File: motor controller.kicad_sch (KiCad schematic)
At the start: 55 parts, among them J1 Servo Header, J2 XT30, J3 Ext Power, J4 USB_PWR, J5 USB Header, J6 M0, J7 M1, J8 M2, J9 M3, M0-BUF1 SN74LVC2G14, M0DA1 LED, M0DB1 LED, M0R1 R_Small, M0R2 R_Small, M1-BUF1 SN74LVC2G14, M1DA1 LED, M1DB1 LED, M1R1 R_Small, M1R2 R_Small, M2-BUF1 SN74LVC2G14, M2DA1 LED, M2DB1 LED, M2R1 R_Small, M2R2 R_Small, M3-BUF1 SN74LVC2G14, M3DA1 LED, M3DB1 LED, M3R1 R_Small, M3R2 R_Small, SW1 SW_Push

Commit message: updated schematic and pcb
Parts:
- J3: footprint Connector_AMASS:AMASS_XT30PW-M_1x02_P2.50mm_Horizontal -> Connector_JST:JST_XH_S3B-XH-A_1x03_P2.50mm_Horizontal
- M0DA1: footprint LED_SMD:LED_0805_2012Metric_Pad1.15x1.40mm_HandSolder -> LED_SMD:LED_0805_2012Metric
- SW1: value SW_Push -> RESET
- U1: renamed from IFX9201SG1; value M1 -> M1-IFX9201SG
- U2: renamed from IFX9201SG2; value M3 -> M3-IFX9201SG
- U3: renamed from IFX9201SG3; value M2 -> M2-IFX9201SG
- U4: renamed from IFX9201SG4; value M0 -> M0-IFX9201SG
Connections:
- net M0-Enc-A: now also M0-BUF1.3 (2A); no longer M0-BUF1.1 (1A)
- net M0-Enc-B: now also M0-BUF1.1 (1A); no longer M0-BUF1.3 (2A)
- net M1-Enc-A: now also M1-BUF1.3 (2A); no longer M1-BUF1.1 (1A)
- net M1-Enc-B: now also M1-BUF1.1 (1A); no longer M1-BUF1.3 (2A)
- net M2-Enc-A: now also M2-BUF1.3 (2A); no longer M2-BUF1.1 (1A)
- net M2-Enc-B: now also M2-BUF1.1 (1A); no longer M2-BUF1.3 (2A)
- net M3-A: now also C19.2; no longer C20.1
- net M3-B: now also C20.1; no longer C19.2
- net M3-Enc-A: now also M3-BUF1.3 (2A); no longer M3-BUF1.1 (1A)
- net M3-Enc-B: now also M3-BUF1.1 (1A); no longer M3-BUF1.3 (2A)
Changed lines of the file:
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@@
 		)
 	)
-	(global_label "M3-Enc-B"
+	(global_label "M3-Enc-A"
 		(shape input)
 		(at 90.17 177.8 180)
@@
 		)
 		(property "Intersheetrefs" "${INTERSHEET_REFS}"
-			(at 76.7225 177.8 0)
+			(at 76.9039 177.8 0)
 			(effects
 				(font
@@
 		)
 	)
-	(global_label "M0-Enc-A"
+	(global_label "M0-Enc-B"
 		(shape input)
 		(at 31.75 137.16 180)
@@
 		)
 		(property "Intersheetrefs" "${INTERSHEET_REFS}"
-			(at 18.4839 137.16 0)
+			(at 18.3025 137.16 0)
 			(effects
 				(font
@@
 		)
 	)
-	(global_label "M1-Enc-B"
+	(global_label "M1-Enc-A"
 		(shape input)
 		(at 90.17 142.24 180)
@@
 		)
 		(property "Intersheetrefs" "${INTERSHEET_REFS}"
-			(at 76.7225 142.24 0)
+			(at 76.9039 142.24 0)
 			(effects
 				(font
@@
 		)
 	)
-	(global_label "M3-B"
+	(global_label "M3-A"
 		(shape input)
 		(at 273.05 143.51 270)
@@
 		)
 		(property "Intersheetrefs" "${INTERSHEET_REFS}"
-			(at 273.05 151.9985 90)
+			(at 273.05 151.8171 90)
 			(effects
 				(font
@@
 		)
 	)
-	(global_label "M3-A"
+	(global_label "M3-B"
 		(shape input)
 		(at 276.86 143.51 270)
@@
 		)
 		(property "Intersheetrefs" "${INTERSHEET_REFS}"
-			(at 276.86 151.8171 90)
+			(at 276.86 151.9985 90)
 			(effects
 				(font
@@
 		)
 	)
-	(global_label "M1-Enc-A"
+	(global_label "M1-Enc-B"
 		(shape input)
 		(at 90.17 137.16 180)
@@
 		)
 		(property "Intersheetrefs" "${INTERSHEET_REFS}"
-			(at 76.9039 137.16 0)
+			(at 76.7225 137.16 0)
 			(effects
 				(font
@@
 		)
 	)
-	(global_label "M2-Enc-A"
+	(global_label "M2-Enc-B"
 		(shape input)
 		(at 31.75 172.72 180)
@@
 		)
 		(property "Intersheetrefs" "${INTERSHEET_REFS}"
-			(at 18.4839 172.72 0)
+			(at 18.3025 172.72 0)
 			(effects
 				(font
@@
 		)
 	)
-	(global_label "M0-Enc-B"
+	(global_label "M0-Enc-A"
 		(shape input)
 		(at 31.75 142.24 180)
@@
 		)
 		(property "Intersheetrefs" "${INTERSHEET_REFS}"
-			(at 18.3025 142.24 0)
+			(at 18.4839 142.24 0)
 			(effects
 				(font
@@
 		)
 	)
-	(global_label "M3-Enc-A"
+	(global_label "M3-Enc-B"
 		(shape input)
 		(at 90.17 172.72 180)
@@
 		)
 		(property "Intersheetrefs" "${INTERSHEET_REFS}"
-			(at 76.9039 172.72 0)
+			(at 76.7225 172.72 0)
 			(effects
 				(font
@@
 		)
 	)
-	(global_label "M2-Enc-B"
+	(global_label "M2-Enc-A"
 		(shape input)
 		(at 31.75 177.8 180)
@@
 		)
 		(property "Intersheetrefs" "${INTERSHEET_REFS}"
-			(at 18.3025 177.8 0)
+			(at 18.4839 177.8 0)
 			(effects
 				(font
@@
 		(on_board yes)
 		(dnp no)
-		(property "Reference" "IFX9201SG3"
+		(property "Reference" "U3"
 			(at 240.03 35.56 0)
 			(effects
@@
 			)
 		)
-		(property "Value" "M2"
+		(property "Value" "M2-IFX9201SG"
 			(at 240.03 52.07 0)
 			(effects
@@
 			(project "motor controller"
 				(path "/0d2d01d1-eff8-45cb-a873-0719ff148ee4"
-					(reference "IFX9201SG3")
+					(reference "U3")
 					(unit 1)
 				)
@@
 			)
 		)
-		(property "Footprint" "LED_SMD:LED_0805_2012Metric_Pad1.15x1.40mm_HandSolder"
+		(property "Footprint" "LED_SMD:LED_0805_2012Metric"
 			(at 64.77 132.08 0)
 			(effects
@@
 		(on_board yes)
 		(dnp no)
-		(property "Reference" "IFX9201SG4"
+		(property "Reference" "U4"
 			(at 240.03 85.09 0)
 			(effects
@@
 			)
 		)
-		(property "Value" "M0"
+		(property "Value" "M0-IFX9201SG"
 			(at 240.03 101.6 0)
 			(effects
@@
 			(project ""
 				(path "/0d2d01d1-eff8-45cb-a873-0719ff148ee4"
-					(reference "IFX9201SG4")
+					(reference "U4")
 					(unit 1)
 				)
@@
 		(on_board yes)
 		(dnp no)
-		(property "Reference" "IFX9201SG2"
+		(property "Reference" "U2"
 			(at 62.23 35.56 0)
 			(effects
@@
 			)
 		)
-		(property "Value" "M3"
+		(property "Value" "M3-IFX9201SG"
 			(at 62.23 52.07 0)
 			(effects
@@
 			(project "motor controller"
 				(path "/0d2d01d1-eff8-45cb-a873-0719ff148ee4"
-					(reference "IFX9201SG2")
+					(reference "U2")
 					(unit 1)
 				)
@@
 		(on_board yes)
 		(dnp no)
-		(property "Reference" "IFX9201SG1"
+		(property "Reference" "U1"
 			(at 60.96 85.09 0)
 			(effects
@@
 			)
 		)
-		(property "Value" "M1"
+		(property "Value" "M1-IFX9201SG"
 			(at 60.96 101.6 0)
 			(effects
@@
 			(project "motor controller"
 				(path "/0d2d01d1-eff8-45cb-a873-0719ff148ee4"
-					(reference "IFX9201SG1")
+					(reference "U1")
 					(unit 1)
 				)
@@
 			)
 		)
-		(property "Value" "SW_Push"
+		(property "Value" "RESET"
 			(at 154.94 118.11 0)
 			(effects
@@
 			)
 		)
-		(property "Footprint" "Connector_AMASS:AMASS_XT30PW-M_1x02_P2.50mm_Horizontal"
+		(property "Footprint" "Connector_JST:JST_XH_S3B-XH-A_1x03_P2.50mm_Horizontal"
 			(at 149.86 142.24 0)
 			(effects

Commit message: changes suggested by Rob
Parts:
- removed C1, C10, C9: 100uF, Capacitor_THT:CP_Radial_D6.3mm_P2.50mm, symbol Device:C_Polarized_Small_US
- removed C17, C18, C19, C20: 10n, Capacitor_SMD:C_1206_3216Metric, symbol Device:C_Small
- C11, C12, C13, C14, C3, C4, C5, C6: value 100n -> 22n
- C15, C16, C7, C8: value 10n -> 22n
- renumbered M3-BUF1 to U5, M0-BUF1 to U6, M2-BUF1 to U7, M1-BUF1 to U8
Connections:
- net +VM is gone; now on net GND: C11.1, C12.1, C2.1, C3.1, C4.1, J2.2 (+), U1.4 (VS), U2.4 (VS), U3.4 (VS), U4.4 (VS)
- net 5v: no longer J3.2 (5v), U5.5 (V_{CC}), U6.5 (V_{CC}), U7.5 (V_{CC}), U8.5 (V_{CC})
- net GND: now also C13.1, C14.1, C15.1, C16.1, C5.2, C6.2, C7.2, C8.2; no longer C2.2, J2.1 (-)
- net M0-A: now also J6.6 (Pin_6); no longer C8.1
- net M0-B: now also J6.5 (Pin_5); no longer C7.2
- net M1-A: now also J7.6 (Pin_6); no longer C16.1
- net M1-B: now also J7.5 (Pin_5); no longer C15.2
- net M2-A: now also J8.6 (Pin_6)
- net M2-B: now also J8.5 (Pin_5)
- net M3-A: now also J9.5 (Pin_5)
- net M3-B: now also J9.6 (Pin_6)
- net M3-Enc-B: no longer J9.1 (Pin_1)
- net +3V3: now reaches C14.2, U3.2 (VSO)
- net +3V3: now also A1.36 (3V3), C13.2, C15.2, C16.2, C5.1, C6.1, C7.1, C8.1, U1.2 (VSO), U2.2 (VSO), U4.2 (VSO), U5.5 (V_{CC}), U6.5 (V_{CC}), U7.5 (V_{CC}), U8.5 (V_{CC})
- net 12v renamed +12V
- removed net 3.3v: A1.36 (3V3), C13.1, C14.1, C5.1, C6.1
- new net: C2.2, J2.1 (-)
- new net +5V: J3.2 (5v)
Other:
- moved on the sheet: J2

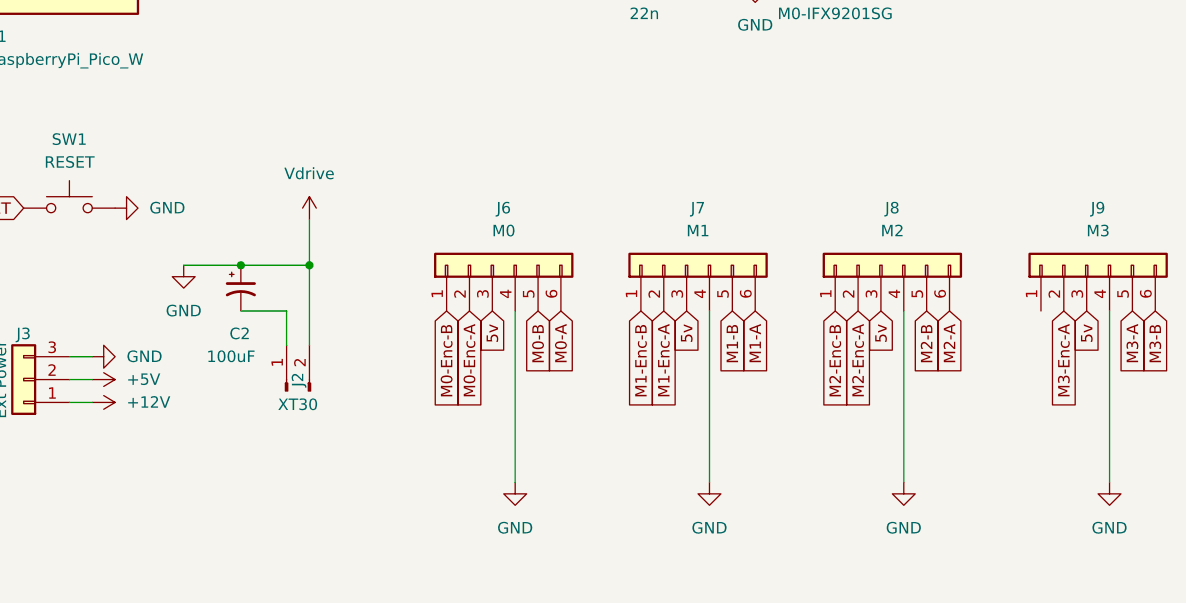
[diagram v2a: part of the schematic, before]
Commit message: fixed a short, started updating the PCB layout
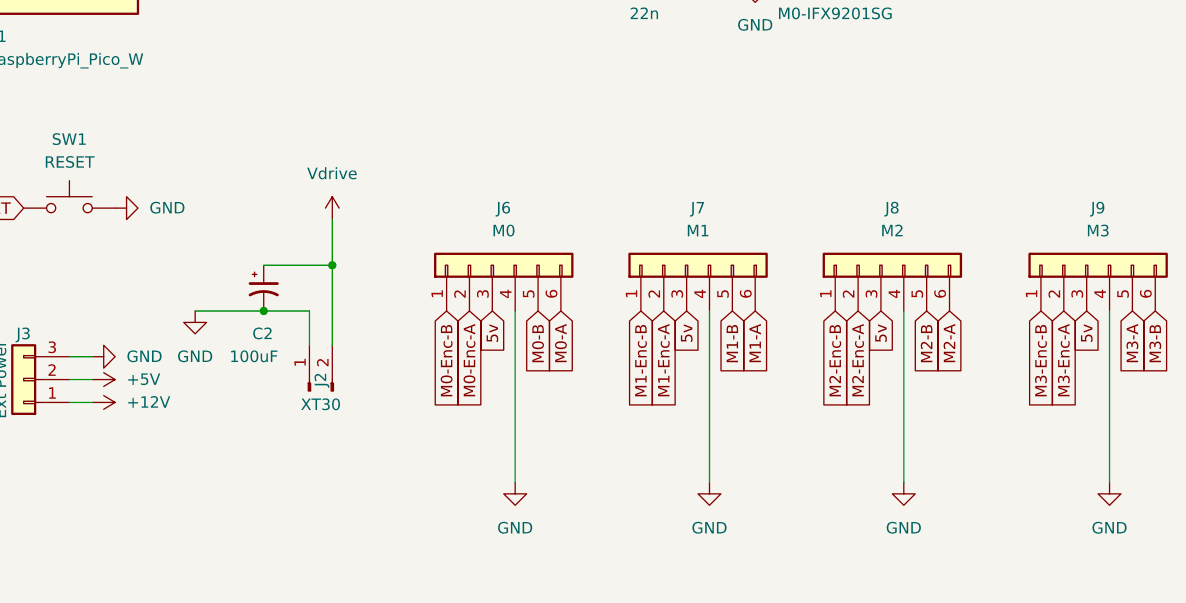
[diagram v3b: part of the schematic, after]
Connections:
- net GND: now also C2.2, J2.1 (-); no longer C11.1, C12.1, C2.1, C3.1, C4.1, J2.2 (+), U1.4 (VS), U2.4 (VS), U3.4 (VS), U4.4 (VS)
- net M3-Enc-B: now also J9.1 (Pin_1)
- new net Vdrive: C11.1, C12.1, C2.1, C3.1, C4.1, J2.2 (+), U1.4 (VS), U2.4 (VS), U3.4 (VS), U4.4 (VS)
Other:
- moved on the sheet: C2, J2
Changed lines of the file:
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@@
 	)
 	(junction
+		(at 176.53 134.62)
+		(diameter 0)
+		(color 0 0 0 0)
+	)
+	(junction
 		(at 218.44 90.17)
 		(diameter 0)
@@
 	)
 	(junction
-		(at 173.99 129.54)
-		(diameter 0)
-		(color 0 0 0 0)
-	)
-	(junction
 		(at 39.37 40.64)
 		(diameter 0)
@@
 	)
 	(junction
-		(at 181.61 129.54)
+		(at 184.15 129.54)
 		(diameter 0)
 		(color 0 0 0 0)
@@
 	(wire
 		(pts
-			(xy 181.61 138.43) (xy 181.61 129.54)
+			(xy 184.15 138.43) (xy 184.15 129.54)
 		)
 		(stroke
@@
 	(wire
 		(pts
-			(xy 181.61 129.54) (xy 181.61 124.46)
+			(xy 184.15 129.54) (xy 184.15 124.46)
 		)
 		(stroke
@@
 	(wire
 		(pts
-			(xy 167.64 129.54) (xy 173.99 129.54)
-		)
-		(stroke
-			(width 0)
-			(type default)
-		)
-	)
-	(wire
-		(pts
 			(xy 111.76 142.24) (xy 111.76 147.32)
 		)
@@
 	(wire
 		(pts
-			(xy 179.07 134.62) (xy 173.99 134.62)
+			(xy 181.61 134.62) (xy 176.53 134.62)
 		)
 		(stroke
@@
 	(wire
 		(pts
-			(xy 179.07 138.43) (xy 179.07 134.62)
+			(xy 168.91 134.62) (xy 176.53 134.62)
+		)
+		(stroke
+			(width 0)
+			(type default)
+		)
+	)
+	(wire
+		(pts
+			(xy 181.61 138.43) (xy 181.61 134.62)
 		)
 		(stroke
@@
 	(wire
 		(pts
-			(xy 173.99 129.54) (xy 181.61 129.54)
+			(xy 176.53 129.54) (xy 184.15 129.54)
 		)
 		(stroke
@@
 		)
 	)
+	(global_label "M3-Enc-B"
+		(shape input)
+		(at 262.89 134.62 270)
+		(fields_autoplaced yes)
+		(effects
+			(font
+				(size 1.27 1.27)
+			)
+			(justify right)
+		)
+		(property "Intersheetrefs" "${INTERSHEET_REFS}"
+			(at 262.89 148.0675 90)
+			(effects
+				(font
+					(size 1.27 1.27)
+				)
+				(justify right)
+				(hide yes)
+			)
+		)
+	)
 	(global_label "PICO RX"
 		(shape input)
@@
 	(symbol
 		(lib_id "power:GND")
-		(at 167.64 129.54 0)
+		(at 168.91 134.62 0)
 		(unit 1)
 		(exclude_from_sim no)
@@
 		(fields_autoplaced yes)
 		(property "Reference" "#PWR045"
-			(at 167.64 135.89 0)
+			(at 168.91 140.97 0)
 			(effects
 				(font
@@
 		)
 		(property "Value" "GND"
-			(at 167.64 134.62 0)
+			(at 168.91 139.7 0)
 			(effects
 				(font
@@
 		)
 		(property "Footprint" ""
-			(at 167.64 129.54 0)
+			(at 168.91 134.62 0)
 			(effects
 				(font
@@
 		)
 		(property "Datasheet" ""
-			(at 167.64 129.54 0)
+			(at 168.91 134.62 0)
 			(effects
 				(font
@@
 		)
 		(property "Description" "Power symbol creates a global label with name \"GND\" , ground"
-			(at 167.64 129.54 0)
+			(at 168.91 134.62 0)
 			(effects
 				(font
@@
 	(symbol
 		(lib_id "power:Vdrive")
-		(at 181.61 124.46 0)
+		(at 184.15 124.46 0)
 		(unit 1)
 		(exclude_from_sim no)
@@
 		(fields_autoplaced yes)
 		(property "Reference" "#PWR046"
-			(at 181.61 128.27 0)
+			(at 184.15 128.27 0)
 			(effects
 				(font
@@
 		)
 		(property "Value" "Vdrive"
-			(at 181.61 119.38 0)
+			(at 184.15 119.38 0)
 			(effects
 				(font
@@
 		)
 		(property "Footprint" ""
-			(at 181.61 124.46 0)
+			(at 184.15 124.46 0)
 			(effects
 				(font
@@
 		)
 		(property "Datasheet" ""
-			(at 181.61 124.46 0)
+			(at 184.15 124.46 0)
 			(effects
 				(font
@@
 		)
 		(property "Description" "Power symbol creates a global label with name \"Vdrive\""
-			(at 181.61 124.46 0)
+			(at 184.15 124.46 0)
 			(effects
 				(font
@@
 	(symbol
 		(lib_id "Connector:Conn_01x02_Pin")
-		(at 179.07 143.51 90)
+		(at 181.61 143.51 90)
 		(unit 1)
 		(exclude_from_sim no)
@@
 		(dnp no)
 		(property "Reference" "J2"
-			(at 180.34 142.24 0)
+			(at 182.88 142.24 0)
 			(effects
 				(font
@@
 		)
 		(property "Value" "XT30"
-			(at 180.34 145.034 90)
+			(at 182.88 145.034 90)
 			(effects
 				(font
@@
 		)
 		(property "Footprint" "Connector_AMASS:AMASS_XT30PW-M_1x02_P2.50mm_Horizontal"
-			(at 179.07 143.51 0)
+			(at 181.61 143.51 0)
 			(effects
 				(font
@@
 		)
 		(property "Datasheet" "~"
-			(at 179.07 143.51 0)
+			(at 181.61 143.51 0)
 			(effects
 				(font
@@
 		)
 		(property "Description" "XT30"
-			(at 179.07 143.51 0)
+			(at 181.61 143.51 0)
 			(effects
 				(font
@@
 	(symbol
 		(lib_id "Device:C_Polarized_Small_US")
-		(at 173.99 132.08 0)
+		(at 176.53 132.08 0)
 		(unit 1)
 		(exclude_from_sim no)
@@
 		(dnp no)
 		(property "Reference" "C2"
-			(at 172.72 137.16 0)
+			(at 175.26 137.16 0)
 			(effects
 				(font
@@
 		)
 		(property "Value" "100uF"
-			(at 170.18 139.7 0)
+			(at 172.72 139.7 0)
 			(effects
 				(font
@@
 		)
 		(property "Footprint" "Capacitor_THT:CP_Radial_D6.3mm_P2.50mm"
-			(at 173.99 132.08 0)
+			(at 176.53 132.08 0)
 			(effects
 				(font
@@
 		)
 		(property "Datasheet" "~"
-			(at 173.99 132.08 0)
+			(at 176.53 132.08 0)
 			(effects
 				(font
@@
 		)
 		(property "Description" "Polarized capacitor, small US symbol"
-			(at 173.99 132.08 0)
+			(at 176.53 132.08 0)
 			(effects
 				(font

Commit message: more tweaking
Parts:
- removed C3, C4, C7, C8: 22n, Capacitor_SMD:C_1206_3216Metric, symbol Device:C_Small
- added C10, C13, C5, C6: 22n, Capacitor_SMD:C_1206_3216Metric, symbol Device:C_Small
- renumbered C13 to C1, C15 to C2, C5 to C3, C6 to C4, C14 to C7, C16 to C8, C2 to C9, J3 to J2, J4 to J3, J5 to J4, J2 to J5, U6 to U1, U7 to U2, U2 to U3, U1 to U4, U8 to U5, U5 to U6, U3 to U7, U4 to U8
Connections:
- net +12V: now also J1.2 (Pin_2); no longer J1.1 (Pin_1)
- net +3V3: now also C11.1, C10.1
- net ADC: now also J1.3 (Pin_3); no longer J1.4 (Pin_4)
- net GND: now also C12.1, J1.1 (Pin_1), C10.2, C13.1, C5.1, C6.1; no longer C12.2, J1.2 (Pin_2)
- net GPIO16: now also M0R2.1, U1.4 (2Y); no longer M0R1.1, U1.6 (1Y)
- net GPIO17: now also M0R1.1, U1.6 (1Y); no longer M0R2.1, U1.4 (2Y)
- net GPIO21: now also M2R1.1, U2.6 (1Y); no longer M2R2.1, U2.4 (2Y)
- net GPIO22: now also M2R2.1, U2.4 (2Y); no longer M2R1.1, U2.6 (1Y)
- net M0-A: now also J6.5 (Pin_5); no longer J6.6 (Pin_6)
- net M0-B: now also J6.6 (Pin_6); no longer J6.5 (Pin_5)
- net M1-A: now also J7.5 (Pin_5); no longer J7.6 (Pin_6)
- net M1-B: now also J7.6 (Pin_6); no longer J7.5 (Pin_5)
- net M1-DIR: now also A1.14 (GPIO10); no longer A1.15 (GPIO11)
- net M1-DIS: now also A1.16 (GPIO12); no longer A1.14 (GPIO10)
- net M1-PWM: now also A1.15 (GPIO11); no longer A1.16 (GPIO12)
- net M1-SO: now also U8.8 (SI)
- net M2-SO: now also U8.3 (SO); no longer U3.8 (SI)
- net SERVO: now also J1.4 (Pin_4); no longer J1.3 (Pin_3)
- net Vdrive: now also C12.2, C13.2, C5.2, C6.2; no longer C11.1, C12.1
- net VBUS: now reaches A1.40 (VBUS), J3.2 (Pin_2)
- net VBUS: now also J6.3 (Pin_3), J7.3 (Pin_3), J8.3 (Pin_3), J9.3 (Pin_3)
- net +5V renamed +5Vext
- net +5Vext: now also J3.3 (Pin_3)
- removed net 5v: J3.3 (Pin_3), J6.3 (Pin_3), J7.3 (Pin_3), J8.3 (Pin_3), J9.3 (Pin_3)
- net M0-SO renamed M3-SO
- net M3-SO: now also U3.3 (SO); no longer U8.3 (SO)
- net PICO RX renamed PICO-RX
- net PICO-RX: no longer U3.3 (SO)
- net PICO TX renamed PICO-TX
- net PICO-TX: now also U3.8 (SI); no longer U8.8 (SI)
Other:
- moved on the sheet: C3, C4, U3, U4, U7, U8

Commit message: switched to vertical plugs
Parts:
- J1, J4: footprint Connector_JST:JST_XH_S4B-XH-A_1x04_P2.50mm_Horizontal -> Connector_JST:JST_XH_B4B-XH-AM_1x04_P2.50mm_Vertical
- J2: footprint Connector_JST:JST_XH_S3B-XH-A_1x03_P2.50mm_Horizontal -> Connector_JST:JST_XH_B3B-XH-AM_1x03_P2.50mm_Vertical
- J6, J7, J8, J9: footprint Connector_JST:JST_XH_S6B-XH-A_1x06_P2.50mm_Horizontal -> Connector_JST:JST_XH_B6B-XH-AM_1x06_P2.50mm_Vertical
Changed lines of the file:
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@@
 			)
 		)
-		(property "Footprint" "Connector_JST:JST_XH_S6B-XH-A_1x06_P2.50mm_Horizontal"
+		(property "Footprint" "Connector_JST:JST_XH_B6B-XH-AM_1x06_P2.50mm_Vertical"
 			(at 267.97 129.54 0)
 			(effects
@@
 			)
 		)
-		(property "Footprint" "Connector_JST:JST_XH_S6B-XH-A_1x06_P2.50mm_Horizontal"
+		(property "Footprint" "Connector_JST:JST_XH_B6B-XH-AM_1x06_P2.50mm_Vertical"
 			(at 245.11 129.54 0)
 			(effects
@@
 			)
 		)
-		(property "Footprint" "Connector_JST:JST_XH_S4B-XH-A_1x04_P2.50mm_Horizontal"
+		(property "Footprint" "Connector_JST:JST_XH_B4B-XH-AM_1x04_P2.50mm_Vertical"
 			(at 179.07 27.94 0)
 			(effects
@@
 			)
 		)
-		(property "Footprint" "Connector_JST:JST_XH_S6B-XH-A_1x06_P2.50mm_Horizontal"
+		(property "Footprint" "Connector_JST:JST_XH_B6B-XH-AM_1x06_P2.50mm_Vertical"
 			(at 201.93 129.54 0)
 			(effects
@@
 			)
 		)
-		(property "Footprint" "Connector_JST:JST_XH_S4B-XH-A_1x04_P2.50mm_Horizontal"
+		(property "Footprint" "Connector_JST:JST_XH_B4B-XH-AM_1x04_P2.50mm_Vertical"
 			(at 101.6 93.98 0)
 			(effects
@@
 			)
 		)
-		(property "Footprint" "Connector_JST:JST_XH_S3B-XH-A_1x03_P2.50mm_Horizontal"
+		(property "Footprint" "Connector_JST:JST_XH_B3B-XH-AM_1x03_P2.50mm_Vertical"
 			(at 149.86 142.24 0)
 			(effects
@@
 			)
 		)
-		(property "Footprint" "Connector_JST:JST_XH_S6B-XH-A_1x06_P2.50mm_Horizontal"
+		(property "Footprint" "Connector_JST:JST_XH_B6B-XH-AM_1x06_P2.50mm_Vertical"
 			(at 223.52 129.54 0)
 			(effects

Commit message: trying again to get the PCB layout to work
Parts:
- J1, J4: footprint Connector_JST:JST_XH_B4B-XH-AM_1x04_P2.50mm_Vertical -> Connector_JST:JST_XH_B4B-XH-A_1x04_P2.50mm_Vertical
- J2: footprint Connector_JST:JST_XH_B3B-XH-AM_1x03_P2.50mm_Vertical -> Connector_JST:JST_XH_B3B-XH-A_1x03_P2.50mm_Vertical
- J6, J7, J8, J9: footprint Connector_JST:JST_XH_B6B-XH-AM_1x06_P2.50mm_Vertical -> Connector_JST:JST_XH_B6B-XH-A_1x06_P2.50mm_Vertical
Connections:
- net M2-A: now also U7.7 (OUT2); no longer U7.5 (OUT1)
- net M2-B: now also U7.5 (OUT1); no longer U7.7 (OUT2)
- net PICO-RX: now also U7.3 (SO)
- net M1-SO: no longer names the net of U4.3 (SO), U8.8 (SI)
- net M1-SO: no longer U7.8 (SI)
- net M2-SO: no longer names the net of U8.3 (SO)
- net M2-SO: now also U7.8 (SI); no longer U7.3 (SO)
- net M3-SO: no longer names the net of U3.3 (SO), U4.8 (SI)
